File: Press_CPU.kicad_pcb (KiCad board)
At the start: 2 copper layers, 40 x 35 mm, 96 parts, among them J2 2-215079-0, U1 APM32F405RGT6, U10 LMV321, U11 LMV321, U12 FM25W256, U13 LMV321, U14 LMV321, U15 LMV321, U16 LMV321, U2 LM2594HVM-3.3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

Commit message: VER1.0: добавил гребенку
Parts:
- added J3: Conn_01x16, PLD_my:PLD16_2.0mm, B.Cu at (163.2, 84.0)
- added J4: Conn_01x16, PLD_my:PLD16_2.0mm, F.Cu at (163.2, 114.0)
- moved D4 2.46 mm to (150.5, 84.8)
- moved D6 2.46 mm to (152.5, 84.8)
- moved D7 2.46 mm to (154.5, 84.8)
- moved R4 2.46 mm to (150.5, 84.8)
- moved R5 2.46 mm to (154.5, 84.8)
- moved R6 2.46 mm to (152.5, 84.8)
- moved C10 2.03 mm to (159.5, 87.2), turned to 90 degrees
- moved C19 2.02 mm to (147.0, 89.5)
- moved D5 2.01 mm to (143.5, 90.2)
- moved L1 2.00 mm to (145.2, 84.8)
- moved C17 1.82 mm to (139.0, 84.5)
- moved U2 1.77 mm to (139.0, 90.0)
- moved R2 1.25 mm to (140.5, 102.8), turned to 90 degrees
- moved C1 1.00 mm to (152.5, 105.5)
- moved C12 1.00 mm to (144.5, 103.0)
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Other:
- board size 40 x 35 mm -> 38.5 x 33 mm
- copper layers 2 -> 4

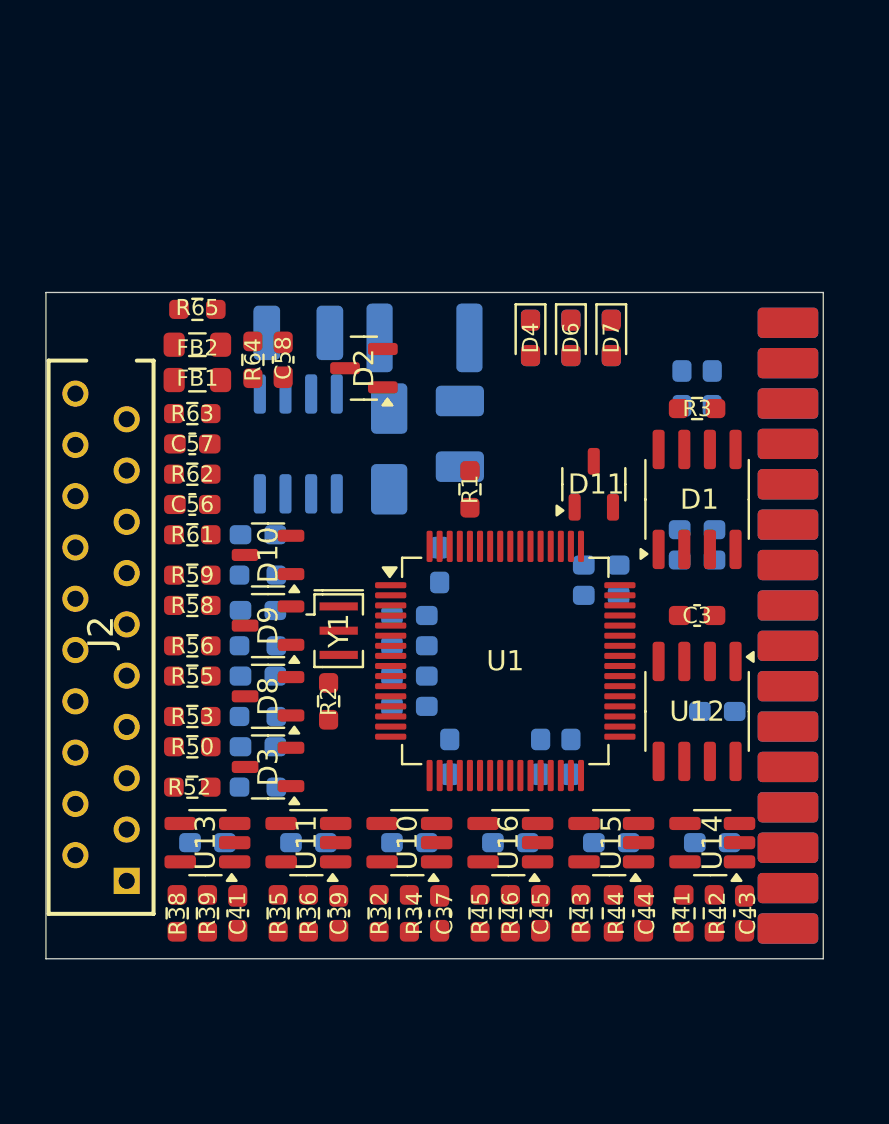
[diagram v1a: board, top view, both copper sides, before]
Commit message: VER1.0: добавил в разъём сигналы
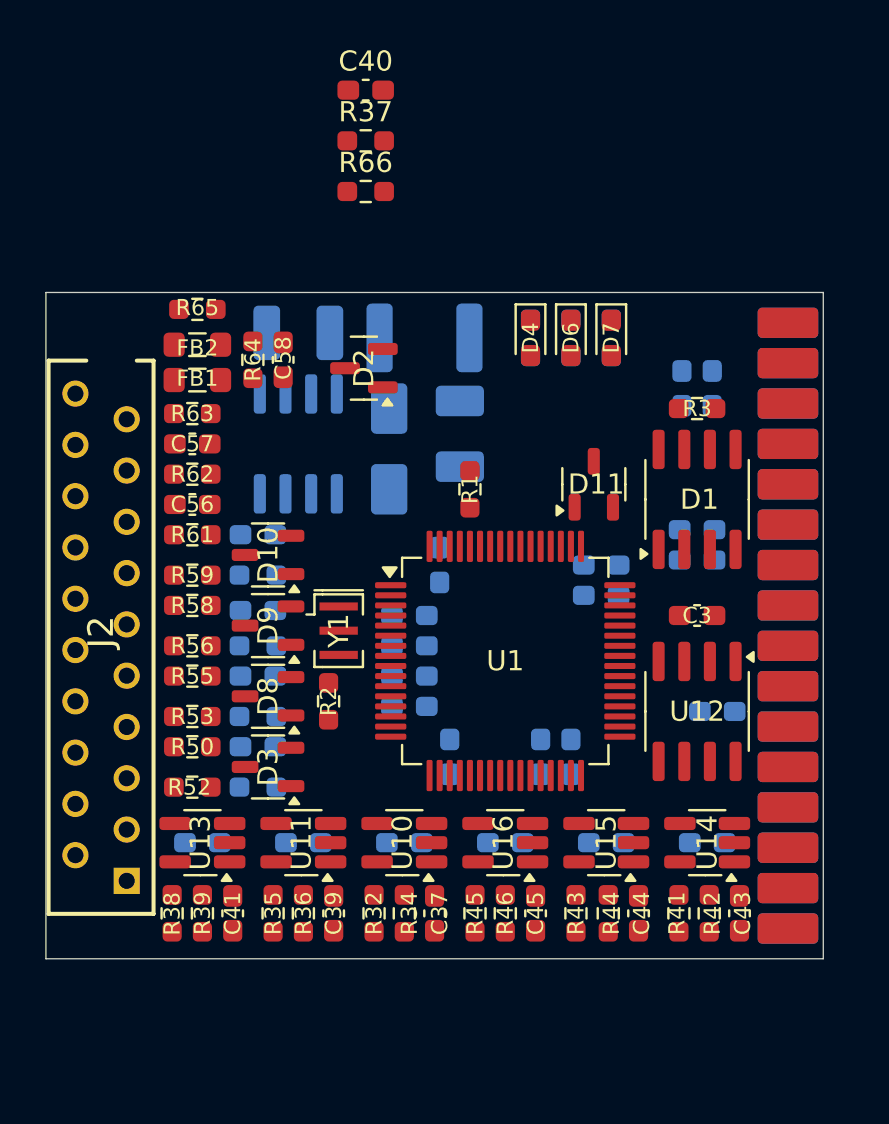
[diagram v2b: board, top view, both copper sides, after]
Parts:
- added C40: 1n, Capacitor_SMD:C_0603_1608Metric_Pad1.08x0.95mm_HandSolder, F.Cu at (142.3, 72.5)
- added R37: 3.6k, Resistor_SMD:R_0603_1608Metric_Pad0.98x0.95mm_HandSolder, F.Cu at (142.3, 75.0)
- added R66: 3.6k, Resistor_SMD:R_0603_1608Metric_Pad0.98x0.95mm_HandSolder, F.Cu at (142.3, 77.5)
- moved C33 0.25 mm to (144.2, 109.8)
- moved C34 0.25 mm to (139.2, 109.8)
- moved C35 0.25 mm to (134.2, 109.8)
- moved C36 0.25 mm to (159.2, 109.8)
- moved C37 0.25 mm to (145.8, 113.2)
- moved C39 0.25 mm to (140.8, 113.2)
- moved C41 0.25 mm to (135.8, 113.2)
- moved C43 0.25 mm to (160.8, 113.2)
- moved C44 0.25 mm to (155.8, 113.2)
- moved C45 0.25 mm to (150.8, 113.2)
- moved C46 0.25 mm to (154.2, 109.8)
- moved C47 0.25 mm to (149.2, 109.8)
- moved R32 0.25 mm to (142.8, 113.2)
- moved R34 0.25 mm to (144.2, 113.2)
- moved R35 0.25 mm to (137.8, 113.2)
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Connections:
- J2 pad 1: unconnected-(J2-Pad1) -> Hall1
- J2 pad 10: unconnected-(J2-Pad10) -> +5V_sense
- J2 pad 11: unconnected-(J2-Pad11) -> GND
- J2 pad 12: unconnected-(J2-Pad12) -> IN/OUT1
- J2 pad 13: unconnected-(J2-Pad13) -> IN/OUT2
- J2 pad 14: unconnected-(J2-Pad14) -> IN/OUT3
- J2 pad 15: unconnected-(J2-Pad15) -> IN/OUT4
- J2 pad 16: unconnected-(J2-Pad16) -> Red_Light+
- J2 pad 17: unconnected-(J2-Pad17) -> Red_Light-
- J2 pad 18: unconnected-(J2-Pad18) -> GND
- J2 pad 19: unconnected-(J2-Pad19) -> SWCLK
- J2 pad 2: unconnected-(J2-Pad2) -> Hall2
- J2 pad 20: unconnected-(J2-Pad20) -> SWDIO
- J2 pad 3: unconnected-(J2-Pad3) -> +5V_sense
- J2 pad 4: unconnected-(J2-Pad4) -> GND
- J2 pad 5: unconnected-(J2-Pad5) -> Hall3
- J2 pad 6: unconnected-(J2-Pad6) -> CANL
- J2 pad 7: unconnected-(J2-Pad7) -> CANH
- J2 pad 8: unconnected-(J2-Pad8) -> CAN_Power
- J2 pad 9: unconnected-(J2-Pad9) -> GND
- J3 pad 1: unconnected-(J3-Pin_1-Pad1) -> VBAT_sense
- J3 pad 10: unconnected-(J3-Pin_10-Pad10) -> +5V
- J3 pad 11: unconnected-(J3-Pin_11-Pad11) -> InH1
- J3 pad 12: unconnected-(J3-Pin_12-Pad12) -> PWM1_H
- J3 pad 13: unconnected-(J3-Pin_13-Pad13) -> InH2
- J3 pad 14: unconnected-(J3-Pin_14-Pad14) -> PWM2_H
- J3 pad 15: unconnected-(J3-Pin_15-Pad15) -> InH3
- J3 pad 16: unconnected-(J3-Pin_16-Pad16) -> PWM3_H
- J3 pad 2: unconnected-(J3-Pin_2-Pad2) -> Temp_mosfet_sense
- J3 pad 3: unconnected-(J3-Pin_3-Pad3) -> Current_C
- J3 pad 4: unconnected-(J3-Pin_4-Pad4) -> Current_B
- J3 pad 5: unconnected-(J3-Pin_5-Pad5) -> Current_A
- J3 pad 6: unconnected-(J3-Pin_6-Pad6) -> +5V_sense
- J3 pad 7: unconnected-(J3-Pin_7-Pad7) -> GND
- J3 pad 8: unconnected-(J3-Pin_8-Pad8) -> uC_drv_en
- J3 pad 9: unconnected-(J3-Pin_9-Pad9) -> GND
- J4 pad 1: unconnected-(J4-Pin_1-Pad1) -> PWM3_L
- J4 pad 10: unconnected-(J4-Pin_10-Pad10) -> GND
- J4 pad 11: unconnected-(J4-Pin_11-Pad11) -> +5V_sense
- J4 pad 12: unconnected-(J4-Pin_12-Pad12) -> Hall3
- J4 pad 13: unconnected-(J4-Pin_13-Pad13) -> Hall2
- J4 pad 14: unconnected-(J4-Pin_14-Pad14) -> Hall1
- J4 pad 15: unconnected-(J4-Pin_15-Pad15) -> Temp_motor_GND
- J4 pad 16: unconnected-(J4-Pin_16-Pad16) -> Temp_motor_sense
- J4 pad 2: unconnected-(J4-Pin_2-Pad2) -> InL3
- J4 pad 3: unconnected-(J4-Pin_3-Pad3) -> PWM2_L
- J4 pad 4: unconnected-(J4-Pin_4-Pad4) -> InL2
- J4 pad 5: unconnected-(J4-Pin_5-Pad5) -> PWM1_L
- J4 pad 6: unconnected-(J4-Pin_6-Pad6) -> InL1
- J4 pad 7: unconnected-(J4-Pin_7-Pad7) -> +5V
- J4 pad 8: unconnected-(J4-Pin_8-Pad8) -> GND
- J4 pad 9: unconnected-(J4-Pin_9-Pad9) -> BkIN

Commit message: VER1.0: промежуточная трассировка
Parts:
- removed C3: 56p, Capacitor_SMD:C_0603_1608Metric_Pad1.08x0.95mm_HandSolder
- added C18: 10u, Capacitor_SMD:C_0805_2012Metric_Pad1.18x1.45mm_HandSolder, B.Cu at (158.2, 96.8)
- C10, C36, C4, C46, C47, U2: moved to F.Cu
- C17: footprint Capacitor_SMD:C_1210_3225Metric_Pad1.33x2.70mm_HandSolder -> Capacitor_SMD:C_0805_2012Metric_Pad1.18x1.45mm_HandSolder
- C37, C39, C41, C56, C57, D2, R1, R32, R34, R35, R36, R38, R39, R62, R63, U10, U11, U12, U13: moved to B.Cu
- moved R38 37.1 mm to (159.8, 87.8), turned to 180 degrees
- moved R39 33.5 mm to (157.2, 88.8)
- moved R35 32.0 mm to (159.8, 90.0), turned to 180 degrees
- moved C41 31.5 mm to (155.6, 88.8)
- moved C35 30.1 mm to (152.8, 86.0), turned to 180 degrees
- moved D6 28.9 mm to (157.6, 113.2)
- moved D4 28.7 mm to (154.0, 113.2)
- moved R4 28.7 mm to (154.0, 113.2)
- moved R6 28.6 mm to (155.8, 113.2)
- moved R5 28.6 mm to (157.6, 113.2)
- moved D7 28.5 mm to (155.8, 113.2)
- moved U13 27.7 mm to (153.0, 89.4), turned to 90 degrees
- moved C40 27.3 mm to (156.2, 96.0), turned to 180 degrees
- moved R32 27.2 mm to (159.8, 92.0), turned to 180 degrees
- moved R37 27.2 mm to (159.6, 96.0)
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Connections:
- J3 pad 11: InH1 -> PWM1_H
- J3 pad 12: PWM1_H -> f1H
- J3 pad 13: InH2 -> PWM2_H
- J3 pad 14: PWM2_H -> f2H
- J3 pad 15: InH3 -> PWM3_H
- J3 pad 16: PWM3_H -> f3H
- J4 pad 1: PWM3_L -> f3L
- J4 pad 2: InL3 -> PWM3_L
- J4 pad 3: PWM2_L -> f2L
- J4 pad 4: InL2 -> PWM2_L
- J4 pad 5: PWM1_L -> f1L
- J4 pad 6: InL1 -> PWM1_L
- R65 pad 1: +5V -> +5V_sense
- U1 pad 20: ADC9 -> EEPROM_~{CS_MCU}
- U1 pad 21: ADC10 -> EEPROM_SCK_MCU
- U1 pad 22: ADC11 -> EEPROM_MISO_MCU
- U1 pad 23: ADC12 -> EEPROM_MOSI_MCU
- U1 pad 33: EEPROM_~{CS_MCU} -> BkIN
- U1 pad 34: EEPROM_SCK_MCU -> PWM1_L
- U1 pad 35: EEPROM_MISO_MCU -> PWM2_L
- U1 pad 36: EEPROM_MOSI_MCU -> PWM3_L
- U1 pad 37: unconnected-(U1-PC6-Pad37) -> f3L
- U1 pad 38: unconnected-(U1-PC7-Pad38) -> f3H
- U1 pad 39: unconnected-(U1-PC8-Pad39) -> f2H
- U1 pad 40: unconnected-(U1-PC9-Pad40) -> f2L
- U1 pad 41: unconnected-(U1-PA8-Pad41) -> PWM1_H
- U1 pad 42: unconnected-(U1-PA9-Pad42) -> PWM2_H
- U1 pad 43: unconnected-(U1-PA10-Pad43) -> PWM3_H
- U1 pad 44: CAN1_RXD_MCU -> f1H
- U1 pad 45: CAN1_TXD_MCU -> f1L
- U1 pad 58: unconnected-(U1-PB6-Pad58) -> uC_drv_en
- U1 pad 61: unconnected-(U1-PB8-Pad61) -> CAN1_RXD_MCU
- U1 pad 62: unconnected-(U1-PB9-Pad62) -> CAN1_TXD_MCU
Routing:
- net GND: track 0.00 -> 94.1 mm, vias 0 -> 36
- net +3.3V: track 0.00 -> 56.1 mm, vias 0 -> 16
- net SWCLK: track 0.00 -> 38.8 mm, vias 0 -> 2
- net SWDIO: track 0.00 -> 38.5 mm, vias 0 -> 2
- net CAN1_RXD_MCU: track 0.00 -> 27.6 mm, vias 0 -> 2
- net EEPROM_~{CS_MCU}: track 0.00 -> 22.5 mm, vias 0 -> 1
- net EEPROM_MISO_MCU: track 0.00 -> 21.7 mm, vias 0 -> 1
- net +5V: track 0.00 -> 21.3 mm, vias 0 -> 2
- net CAN1_TXD_MCU: track 0.00 -> 20.8 mm, vias 0 -> 2
- net uC_drv_en: track 0.00 -> 19.5 mm, vias 0 -> 1
- net BkIN: track 0.00 -> 19.4 mm, vias 0 -> 2
- net Net-(U11-+): track 0.00 -> 18.8 mm
- net CANH: track 0.00 -> 18.0 mm
- net PWM1_L: track 0.00 -> 17.5 mm, vias 0 -> 2
- net PWM3_H: track 0.00 -> 17.4 mm, vias 0 -> 1
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- added copper zone on In1.Cu, net +3.3V
- added copper zone on B.Cu, net GND
- added copper zone on F.Cu, net GND
- added copper zone on In2.Cu, net GND

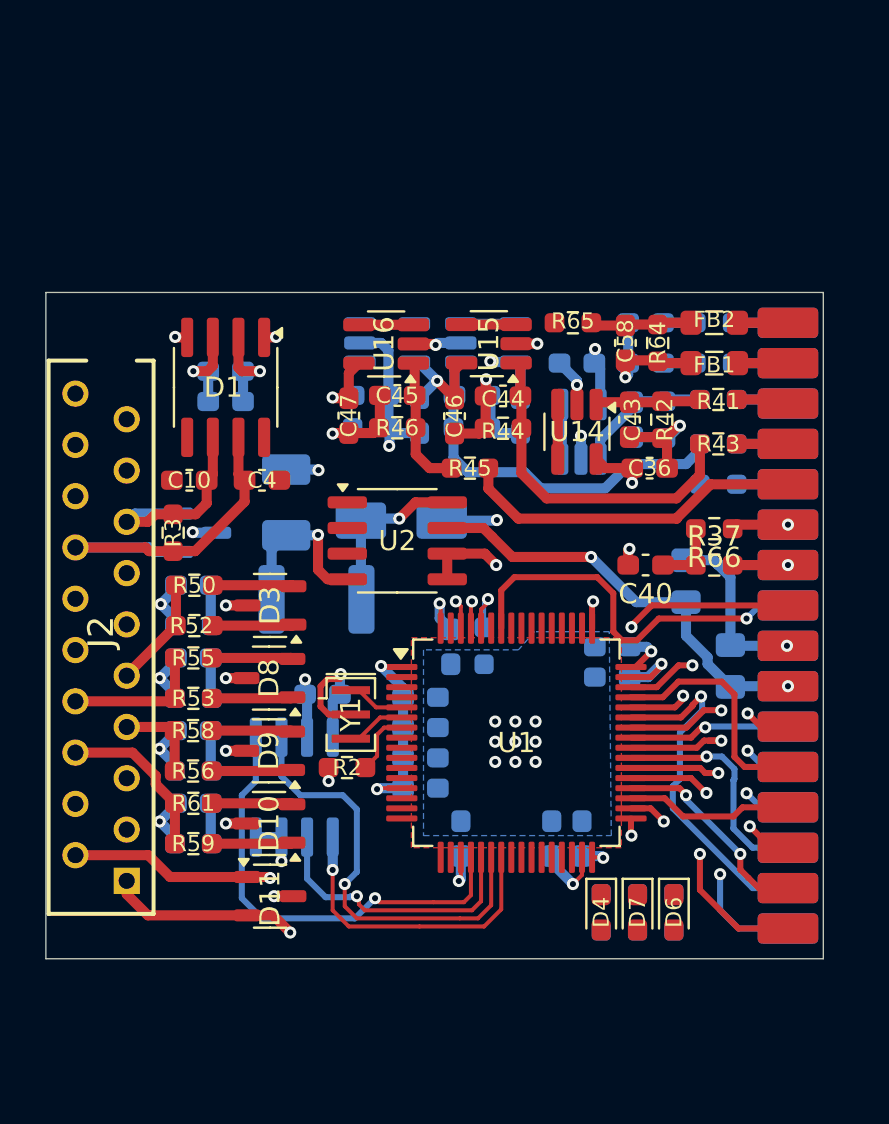
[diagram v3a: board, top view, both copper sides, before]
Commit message: VER1.0: попробовал развести по другому
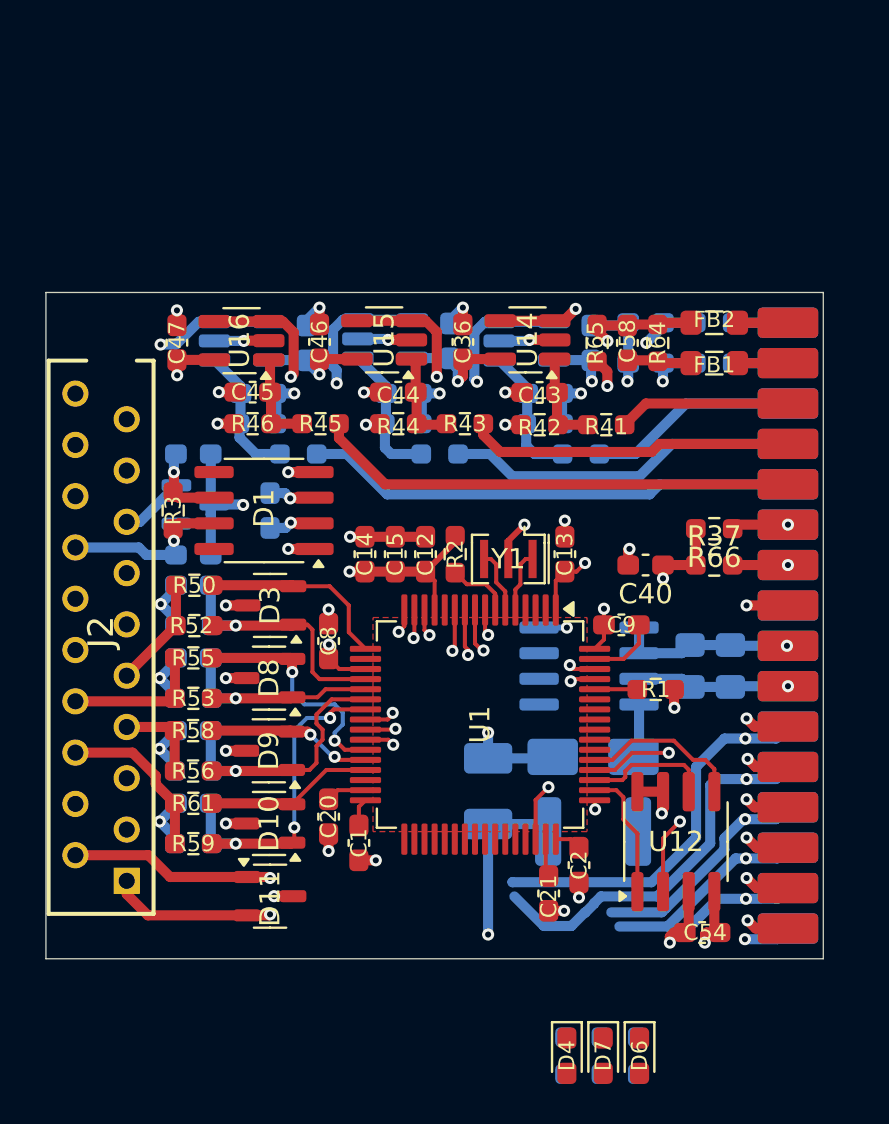
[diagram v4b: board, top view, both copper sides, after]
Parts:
- removed C7: 1u, Capacitor_SMD:C_0603_1608Metric_Pad1.08x0.95mm_HandSolder
- C1, C12, C13, C14, C15, C2, C20, C21, C54, C8, C9, R1, U12: moved to F.Cu
- C10, C4, U2: moved to B.Cu
- C6: value 1u -> 2.2u
- moved C54 22.2 mm to (159.0, 114.2)
- moved R32 20.9 mm to (139.0, 90.5)
- moved U12 19.1 mm to (157.7, 109.7), turned to 90 degrees
- moved L1 17.9 mm to (153.6, 109.2)
- moved C19 17.4 mm to (148.4, 107.2)
- moved D5 15.1 mm to (153.6, 105.5), turned to 180 degrees
- moved R35 13.8 mm to (146.0, 90.5)
- moved R43 12.6 mm to (147.2, 89.0)
- moved R2 11.8 mm to (146.8, 95.5), turned to -90 degrees
- moved C8 11.8 mm to (140.5, 99.8)
- moved C12 11.6 mm to (145.3, 95.5), turned to 90 degrees
- moved U2 11.3 mm to (153.4, 101.0)
- moved C21 11.2 mm to (151.4, 112.3), turned to -90 degrees
- moved C36 11.2 mm to (147.2, 85.0), turned to 90 degrees
- moved C20 11.1 mm to (140.5, 108.5), turned to -90 degrees
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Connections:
- U1 pad 10: ADC3 -> Current_B_MCU
- U1 pad 11: ADC4 -> Current_C_MCU
- U1 pad 14: ADC5 -> Hall3_MCU
- U1 pad 15: ADC6 -> Hall1_MCU
- U1 pad 16: ADC7 -> Hall2_MCU
- U1 pad 17: ADC8 -> DigIN1_MCU
- U1 pad 20: EEPROM_~{CS_MCU} -> AnalogIN1_MCU
- U1 pad 21: EEPROM_SCK_MCU -> AnalogIN2_MCU
- U1 pad 22: EEPROM_MISO_MCU -> AnalogIN3_MCU
- U1 pad 23: EEPROM_MOSI_MCU -> AnalogIN4_MCU
- U1 pad 24: ADC13 -> VBAT_sense_MCU
- U1 pad 25: ADC14 -> Temp_motor_sense_MCU
- U1 pad 26: ADC15 -> Temp_mosfet_sense_MCU
- U1 pad 27: ADC16 -> DigIN2_MCU
- U1 pad 28: unconnected-(U1-PB2-Pad28) -> DigIN3_MCU
- U1 pad 29: unconnected-(U1-PB10-Pad29) -> DigIN4_MCU
- U1 pad 50: unconnected-(U1-PA15-Pad50) -> EEPROM_~{CS_MCU}
- U1 pad 51: unconnected-(U1-PC10-Pad51) -> EEPROM_SCK_MCU
- U1 pad 52: unconnected-(U1-PC11-Pad52) -> EEPROM_MISO_MCU
- U1 pad 53: unconnected-(U1-PC12-Pad53) -> EEPROM_MOSI_MCU
- U1 pad 8: ADC1 -> +5V_sense_MCU
- U1 pad 9: ADC2 -> Current_A_MCU
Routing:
- net Current_A_MCU: track 0.00 -> 36.8 mm, vias 0 -> 2
- net VBAT_sense_MCU: track 1.62 -> 35.9 mm, vias 0 -> 2
- net Temp_mosfet_sense_MCU: track 1.62 -> 34.2 mm, vias 0 -> 2
- net Temp_motor_sense_MCU: track 5.05 -> 32.3 mm, vias 0 -> 2
- net Current_B_MCU: track 2.70 -> 28.2 mm, vias 0 -> 2
- net Hall3_MCU: track 2.70 -> 26.1 mm, vias 0 -> 2
- net Hall1_MCU: track 2.70 -> 25.0 mm, vias 0 -> 2
- net Current_A: track 2.54 -> 24.4 mm
- net Current_C_MCU: track 2.70 -> 22.6 mm, vias 0 -> 2
- net uC_drv_en: track 19.5 -> 0.00 mm, vias 1 -> 0
- net Hall2_MCU: track 2.70 -> 21.1 mm, vias 0 -> 2
- net BkIN: track 19.4 -> 2.05 mm, vias 2 -> 1
- net EEPROM_~{CS_MCU}: track 22.5 -> 6.53 mm, vias 1 -> 0
- net +5V_sense: track 2.82 -> 18.4 mm, vias 1 -> 2
- net PWM1_L: track 17.5 -> 2.22 mm, vias 2 -> 1
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- removed copper zone on B.Cu, net GND

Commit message: VER1.0: первая готовая трассировка, требует обсуждения
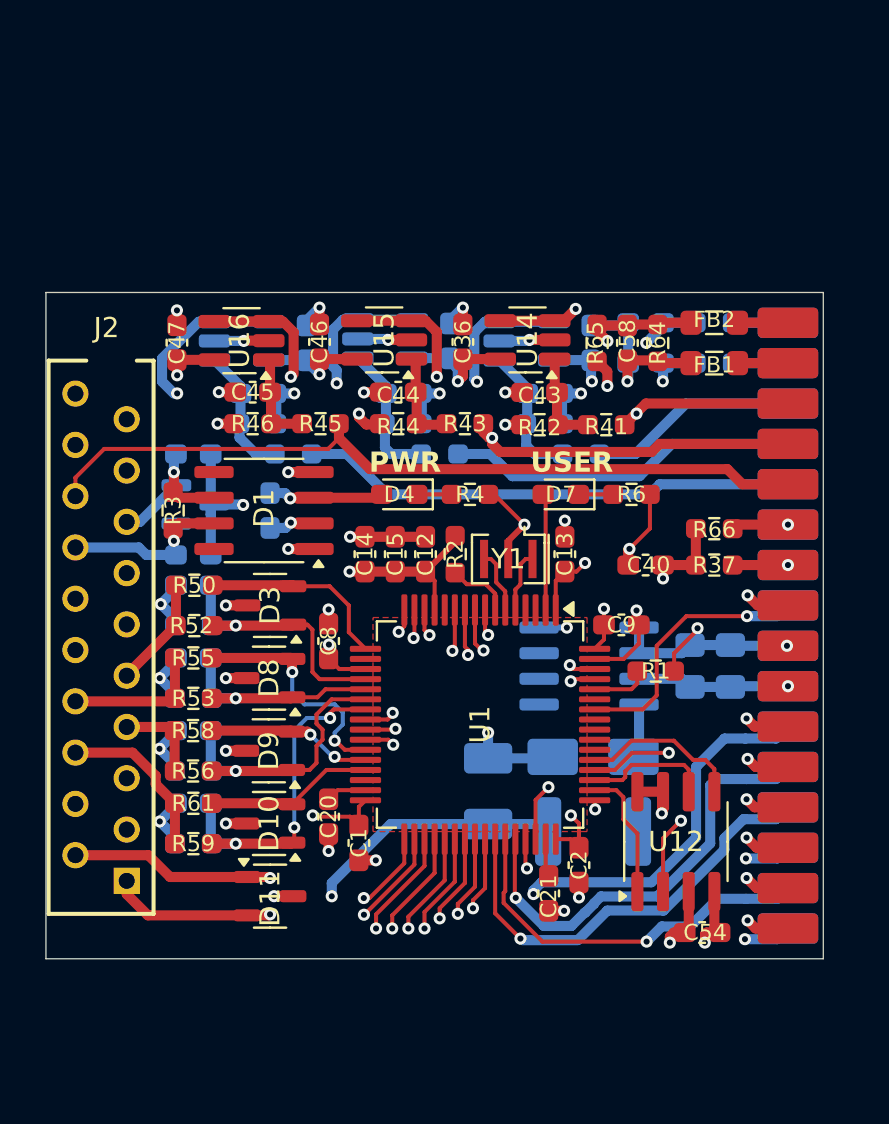
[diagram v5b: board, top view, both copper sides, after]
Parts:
- removed D6: ~, LED_SMD:LED_0603_1608Metric_Pad1.05x0.95mm_HandSolder
- removed R5: 1k, Resistor_SMD:R_0603_1608Metric_Pad0.98x0.95mm_HandSolder
- R4, R6: moved to F.Cu
- moved D4 29.0 mm to (144.0, 92.5), turned to 180 degrees
- moved R4 28.2 mm to (147.5, 92.5), turned to 0 degrees
- moved D7 27.9 mm to (152.0, 92.5), turned to 180 degrees
- moved R6 27.8 mm to (155.5, 92.5), turned to 0 degrees
- moved R1 0.91 mm to (156.7, 101.2)
- moved R32 0.25 mm to (138.8, 90.5)
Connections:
- J2 pad 10: +5V_sense -> +5V
- J2 pad 3: +5V_sense -> +5V
- J3 pad 6: +5V_sense -> +5V
- J4 pad 11: +5V_sense -> +5V
- R65 pad 1: +5V_sense -> +5V
- R66 pad 1: +5V_sense -> +5V
- U1 pad 2: unconnected-(U1-PC13-Pad2) -> Net-(D7-A)
- U1 pad 56: Net-(D7-A) -> unconnected-(U1-PB4-Pad56)
- U1 pad 57: Net-(D6-A) -> unconnected-(U1-PB5-Pad57)
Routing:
- net +5V: track 7.56 -> 79.5 mm, vias 1 -> 3
- net Hall1: track 8.81 -> 42.2 mm, vias 0 -> 1
- net BkIN: track 2.05 -> 33.8 mm, vias 1 -> 2
- net Hall2: track 16.2 -> 45.8 mm, vias 0 -> 1
- net PWM1_L: track 2.22 -> 30.0 mm, vias 1 -> 2
- net PWM2_L: track 2.22 -> 28.7 mm, vias 1 -> 2
- net PWM3_L: track 2.26 -> 26.2 mm, vias 1 -> 2
- net f3L: track 2.17 -> 25.0 mm, vias 1 -> 2
- net f3H: track 2.35 -> 23.9 mm, vias 1 -> 2
- net f2L: track 2.26 -> 22.4 mm, vias 1 -> 2
- net +5V_sense: track 18.4 -> 0.00 mm, vias 2 -> 0
- net f1L: track 2.17 -> 17.0 mm, vias 1 -> 2
- net Hall3: track 23.9 -> 38.7 mm
- net f2H: track 9.97 -> 24.1 mm, vias 1 -> 2
- net PWM3_H: track 5.64 -> 19.2 mm
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- added copper zone on In3.Cu, net +3.3V
- added copper zone on In4.Cu, net GND
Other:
- copper layers 4 -> 6
- board text added: "PWR"
- board text added: "USER"
